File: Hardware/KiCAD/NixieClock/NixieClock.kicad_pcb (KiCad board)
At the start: 2 copper layers, 7 parts

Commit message: KiCAD Progress
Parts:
- removed REF** (x2): DIP-16_W10.16mm, Package_DIP:DIP-16_W10.16mm
- J0, J1: renamed from REF**; value Molex_Mini-Fit_Jr_5566-12A_2x06_P4.20mm_Vertical -> (none)
- moved IC0 0.49 mm to (55.3, 58.4)
- moved IC2 0.49 mm to (15.3, 58.4)
- moved IC1 0.49 mm to (35.7, 78.7)
- renumbered REF** to IC0, REF** to IC1, REF** to IC2
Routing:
- net (no net): track 4.03 -> 143.6 mm, vias 0 -> 1

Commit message: progress
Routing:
- net (no net): track 143.6 -> 300.5 mm

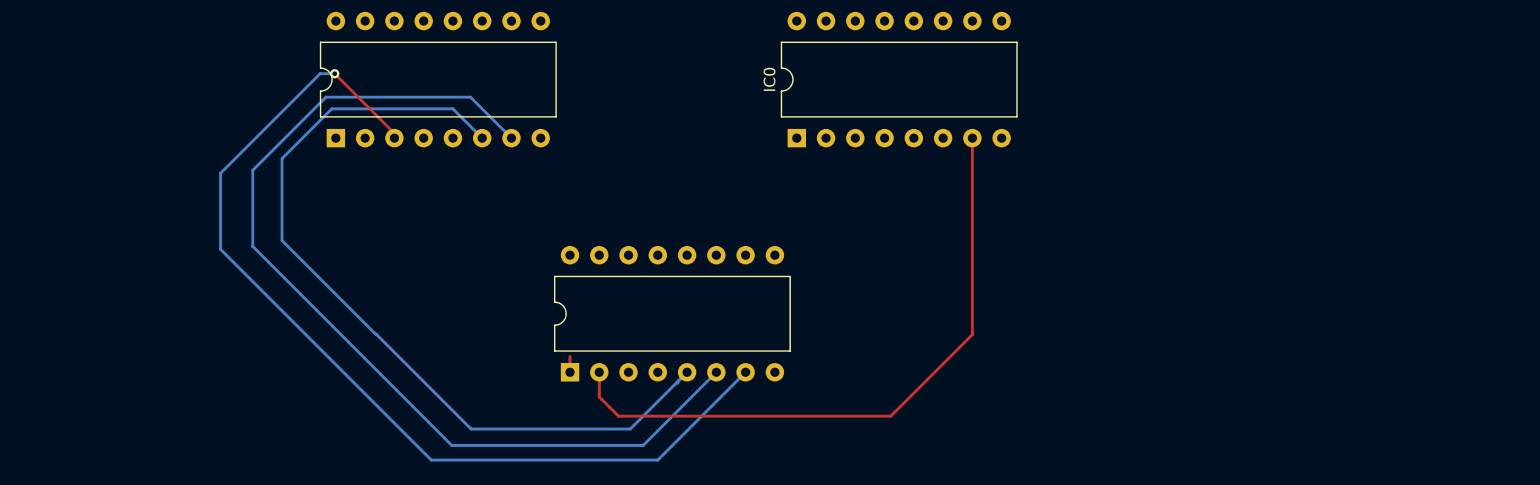
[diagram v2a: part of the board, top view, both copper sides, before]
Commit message: Routed from one shift register to BCD.. removed gound and vcc on eagle
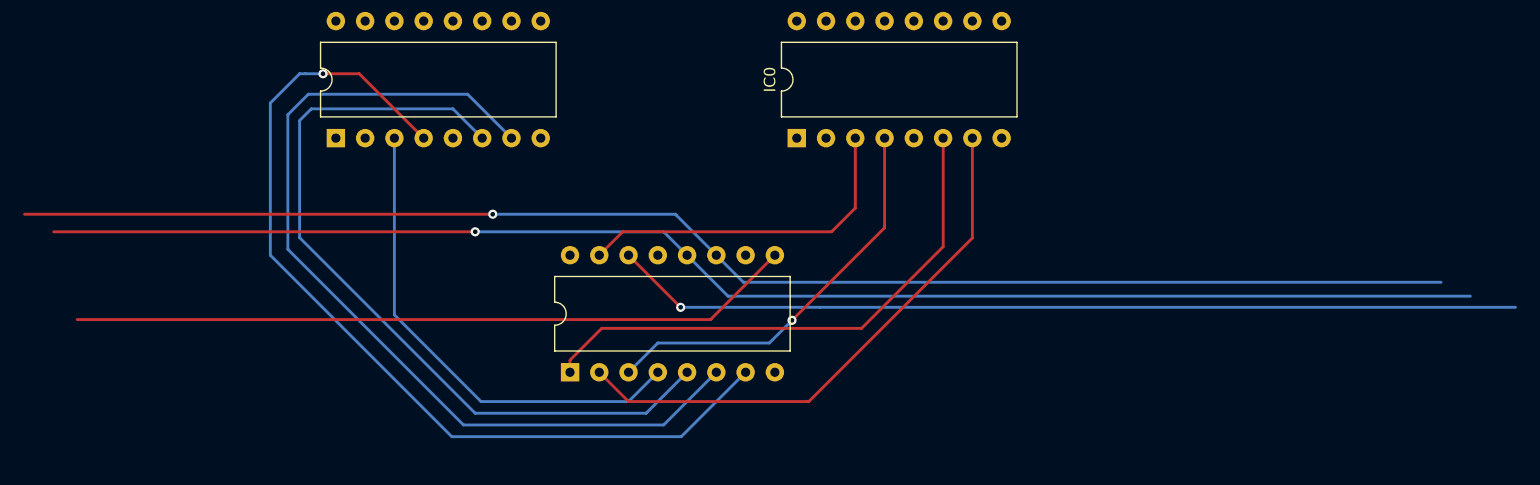
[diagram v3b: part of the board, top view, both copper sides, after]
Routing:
- net (no net): track 300.5 -> 827.0 mm, vias 1 -> 5
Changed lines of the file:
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@@
-(kicad_pcb (version 20171130) (host pcbnew "(5.1.4-0-10_14)")
+(kicad_pcb (version 20171130) (host pcbnew "(5.1.4)-1")
   (general
     (thickness 1.6)
     (drawings 0)
-    (tracks 36)
+    (tracks 73)
     (zones 0)
     (modules 5)
@@
   (segment (start 22.14 33.43) (end 23.74 33.43) (width 0.25) (layer F.Cu) (net 0))
   (segment (start 20.42 35.15) (end 22.14 33.43) (width 0.25) (layer F.Cu) (net 0))
-  (via (at 15.24 52.832) (size 0.8) (drill 0.4) (layers F.Cu B.Cu) (net 0))
-  (segment (start 45.020001 79.539999) (end 45.020001 79.693999) (width 0.25) (layer B.Cu) (net 0))
-  (segment (start 45.82 78.74) (end 45.020001 79.539999) (width 0.25) (layer B.Cu) (net 0))
-  (segment (start 13.97 52.832) (end 15.24 52.832) (width 0.25) (layer B.Cu) (net 0))
-  (segment (start 5.334 68.072) (end 5.334 61.468) (width 0.25) (layer B.Cu) (net 0))
-  (segment (start 23.622 86.36) (end 5.334 68.072) (width 0.25) (layer B.Cu) (net 0))
-  (segment (start 5.334 61.468) (end 13.97 52.832) (width 0.25) (layer B.Cu) (net 0))
-  (segment (start 43.28 86.36) (end 23.622 86.36) (width 0.25) (layer B.Cu) (net 0))
-  (segment (start 50.9 78.74) (end 43.28 86.36) (width 0.25) (layer B.Cu) (net 0))
-  (segment (start 8.128 61.214) (end 14.478 54.864) (width 0.25) (layer B.Cu) (net 0))
-  (segment (start 8.128 67.818) (end 8.128 61.214) (width 0.25) (layer B.Cu) (net 0))
-  (segment (start 42.01 85.09) (end 25.4 85.09) (width 0.25) (layer B.Cu) (net 0))
-  (segment (start 25.4 85.09) (end 8.128 67.818) (width 0.25) (layer B.Cu) (net 0))
-  (segment (start 48.36 78.74) (end 42.01 85.09) (width 0.25) (layer B.Cu) (net 0))
-  (segment (start 14.986 55.88) (end 25.5 55.88) (width 0.25) (layer B.Cu) (net 0))
-  (segment (start 10.668 67.31) (end 10.668 60.198) (width 0.25) (layer B.Cu) (net 0))
-  (segment (start 18.85 75.438) (end 18.796 75.438) (width 0.25) (layer B.Cu) (net 0))
-  (segment (start 27.078 83.666) (end 18.85 75.438) (width 0.25) (layer B.Cu) (net 0))
-  (segment (start 18.796 75.438) (end 10.668 67.31) (width 0.25) (layer B.Cu) (net 0))
+  (via (at 14.224 52.832) (size 0.8) (drill 0.4) (layers F.Cu B.Cu) (net 0))
+  (segment (start 20.42 58.012) (end 20.42 58.42) (width 0.25) (layer F.Cu) (net 0))
+  (segment (start 26.77 54.61) (end 30.58 58.42) (width 0.25) (layer B.Cu) (net 0))
+  (segment (start 43.28 78.74) (end 40.74 81.28) (width 0.25) (layer B.Cu) (net 0))
+  (segment (start 20.42 73.76) (end 20.42 58.42) (width 0.25) (layer B.Cu) (net 0))
+  (segment (start 17.372 52.832) (end 22.96 58.42) (width 0.25) (layer F.Cu) (net 0))
+  (segment (start 68.04 67.85) (end 68.04 58.42) (width 0.25) (layer F.Cu) (net 0))
+  (segment (start 60.96 74.93) (end 68.04 67.85) (width 0.25) (layer F.Cu) (net 0))
+  (segment (start 38.42 74.93) (end 60.96 74.93) (width 0.25) (layer F.Cu) (net 0))
+  (segment (start 35.66 78.74) (end 35.66 77.69) (width 0.25) (layer F.Cu) (net 0))
+  (segment (start 35.66 77.69) (end 38.42 74.93) (width 0.25) (layer F.Cu) (net 0))
+  (segment (start 45.312 73.152) (end 45.262 73.102) (width 0.25) (layer F.Cu) (net 0))
+  (segment (start 45.82 68.58) (end 43.788 66.548) (width 0.25) (layer B.Cu) (net 0))
+  (segment (start 43.788 66.548) (end 27.432 66.548) (width 0.25) (layer B.Cu) (net 0))
+  (via (at 27.432 66.548) (size 0.8) (drill 0.4) (layers F.Cu B.Cu) (net 0))
+  (segment (start 27.432 66.548) (end -9.144 66.548) (width 0.25) (layer F.Cu) (net 0))
+  (via (at 28.956 65.024) (size 0.8) (drill 0.4) (layers F.Cu B.Cu) (net 0))
+  (segment (start 28.956 65.024) (end -11.684 65.024) (width 0.25) (layer F.Cu) (net 0))
+  (segment (start 40.74 81.28) (end 38.2 78.74) (width 0.25) (layer F.Cu) (net 0))
+  (segment (start 40.74 78.74) (end 43.28 76.2) (width 0.25) (layer B.Cu) (net 0))
+  (via (at 54.9275 74.2315) (size 0.8) (drill 0.4) (layers F.Cu B.Cu) (net 0))
+  (segment (start 40.74 81.28) (end 56.388 81.28) (width 0.25) (layer F.Cu) (net 0))
+  (segment (start 70.58 67.088) (end 70.58 58.42) (width 0.25) (layer F.Cu) (net 0))
+  (segment (start 56.388 81.28) (end 70.58 67.088) (width 0.25) (layer F.Cu) (net 0))
+  (segment (start 48.36 78.74) (end 43.788 83.312) (width 0.25) (layer B.Cu) (net 0))
+  (segment (start 43.788 83.312) (end 26.416 83.312) (width 0.25) (layer B.Cu) (net 0))
+  (segment (start 26.416 83.312) (end 11.176 68.072) (width 0.25) (layer B.Cu) (net 0))
+  (segment (start 11.176 56.388) (end 12.954 54.61) (width 0.25) (layer B.Cu) (net 0))
+  (segment (start 11.176 68.072) (end 11.176 56.388) (width 0.25) (layer B.Cu) (net 0))
+  (segment (start 12.954 54.61) (end 26.77 54.61) (width 0.25) (layer B.Cu) (net 0))
+  (segment (start 17.372 52.832) (end 14.224 52.832) (width 0.25) (layer F.Cu) (net 0))
+  (segment (start 45.262 73.102) (end 40.74 68.58) (width 0.25) (layer F.Cu) (net 0))
+  (via (at 45.262 73.102) (size 0.8) (drill 0.4) (layers F.Cu B.Cu) (net 0))
+  (segment (start 47.879 74.141) (end 47.879 74.168) (width 0.25) (layer F.Cu) (net 0))
+  (segment (start 53.44 68.58) (end 47.879 74.141) (width 0.25) (layer F.Cu) (net 0))
+  (segment (start 47.879 74.168) (end -7.112 74.168) (width 0.25) (layer F.Cu) (net 0))
+  (segment (start 27.94 81.28) (end 20.42 73.76) (width 0.25) (layer B.Cu) (net 0))
+  (segment (start 40.74 81.28) (end 27.94 81.28) (width 0.25) (layer B.Cu) (net 0))
   (segment (start 25.5 55.88) (end 28.04 58.42) (width 0.25) (layer B.Cu) (net 0))
-  (segment (start 10.668 60.198) (end 14.986 55.88) (width 0.25) (layer B.Cu) (net 0))
-  (segment (start 40.894 83.666) (end 27.078 83.666) (width 0.25) (layer B.Cu) (net 0))
-  (segment (start 45.82 78.74) (end 40.894 83.666) (width 0.25) (layer B.Cu) (net 0))
-  (segment (start 27.024 54.864) (end 30.58 58.42) (width 0.25) (layer B.Cu) (net 0))
-  (segment (start 14.478 54.864) (end 27.024 54.864) (width 0.25) (layer B.Cu) (net 0))
-  (segment (start 20.42 58.012) (end 20.42 58.42) (width 0.25) (layer F.Cu) (net 0))
-  (segment (start 15.24 52.832) (end 20.42 58.012) (width 0.25) (layer F.Cu) (net 0))
-  (segment (start 35.66 78.74) (end 35.66 77.37) (width 0.25) (layer F.Cu) (net 0))
-  (segment (start 63.5 82.55) (end 39.878 82.55) (width 0.25) (layer F.Cu) (net 0))
-  (segment (start 70.58 75.406) (end 70.612 75.438) (width 0.25) (layer F.Cu) (net 0))
-  (segment (start 39.878 82.55) (end 38.2 80.872) (width 0.25) (layer F.Cu) (net 0))
-  (segment (start 70.612 75.438) (end 63.5 82.55) (width 0.25) (layer F.Cu) (net 0))
-  (segment (start 38.2 80.872) (end 38.2 78.74) (width 0.25) (layer F.Cu) (net 0))
-  (segment (start 70.58 58.42) (end 70.58 75.406) (width 0.25) (layer F.Cu) (net 0))
+  (segment (start 42.264 82.296) (end 27.432 82.296) (width 0.25) (layer B.Cu) (net 0))
+  (segment (start 45.82 78.74) (end 42.264 82.296) (width 0.25) (layer B.Cu) (net 0))
+  (segment (start 27.432 82.296) (end 12.192 67.056) (width 0.25) (layer B.Cu) (net 0))
+  (segment (start 12.192 67.056) (end 12.192 56.896) (width 0.25) (layer B.Cu) (net 0))
+  (segment (start 12.192 56.896) (end 13.208 55.88) (width 0.25) (layer B.Cu) (net 0))
+  (segment (start 13.208 55.88) (end 25.5 55.88) (width 0.25) (layer B.Cu) (net 0))
+  (segment (start 12.7 52.832) (end 14.224 52.832) (width 0.25) (layer B.Cu) (net 0))
+  (segment (start 45.312 84.328) (end 25.4 84.328) (width 0.25) (layer B.Cu) (net 0))
+  (segment (start 50.9 78.74) (end 45.312 84.328) (width 0.25) (layer B.Cu) (net 0))
+  (segment (start 25.4 84.328) (end 9.652 68.58) (width 0.25) (layer B.Cu) (net 0))
+  (segment (start 9.652 68.58) (end 9.652 55.372) (width 0.25) (layer B.Cu) (net 0))
+  (segment (start 9.652 55.372) (end 12.192 52.832) (width 0.25) (layer B.Cu) (net 0))
+  (segment (start 12.192 52.832) (end 12.7 52.832) (width 0.25) (layer B.Cu) (net 0))
+  (segment (start 45.262 73.102) (end 57.354 73.102) (width 0.25) (layer B.Cu) (net 0))
+  (segment (start 57.354 73.102) (end 117.7155 73.102) (width 0.25) (layer B.Cu) (net 0))
+  (segment (start 52.959 76.2) (end 54.9275 74.2315) (width 0.25) (layer B.Cu) (net 0))
+  (segment (start 43.28 76.2) (end 52.959 76.2) (width 0.25) (layer B.Cu) (net 0))
+  (segment (start 62.96 66.199) (end 62.96 66.072) (width 0.25) (layer F.Cu) (net 0))
+  (segment (start 54.9275 74.2315) (end 62.96 66.199) (width 0.25) (layer F.Cu) (net 0))
+  (segment (start 62.96 66.072) (end 62.96 58.42) (width 0.25) (layer F.Cu) (net 0))
+  (segment (start 60.42 64.484) (end 60.42 58.42) (width 0.25) (layer F.Cu) (net 0))
+  (segment (start 58.356 66.548) (end 60.42 64.484) (width 0.25) (layer F.Cu) (net 0))
+  (segment (start 38.2 68.58) (end 40.232 66.548) (width 0.25) (layer F.Cu) (net 0))
+  (segment (start 40.232 66.548) (end 58.356 66.548) (width 0.25) (layer F.Cu) (net 0))
+  (segment (start 49.376 72.136) (end 49.911 72.136) (width 0.25) (layer B.Cu) (net 0))
+  (segment (start 45.82 68.58) (end 49.376 72.136) (width 0.25) (layer B.Cu) (net 0))
+  (segment (start 49.911 72.136) (end 113.792 72.136) (width 0.25) (layer B.Cu) (net 0))
+  (segment (start 48.36 68.58) (end 50.7095 70.9295) (width 0.25) (layer B.Cu) (net 0))
+  (segment (start 50.7095 70.9295) (end 111.252 70.9295) (width 0.25) (layer B.Cu) (net 0))
+  (segment (start 44.804 65.024) (end 44.881 65.101) (width 0.25) (layer B.Cu) (net 0))
+  (segment (start 28.956 65.024) (end 44.804 65.024) (width 0.25) (layer B.Cu) (net 0))
+  (segment (start 48.36 68.58) (end 44.881 65.101) (width 0.25) (layer B.Cu) (net 0))
 )

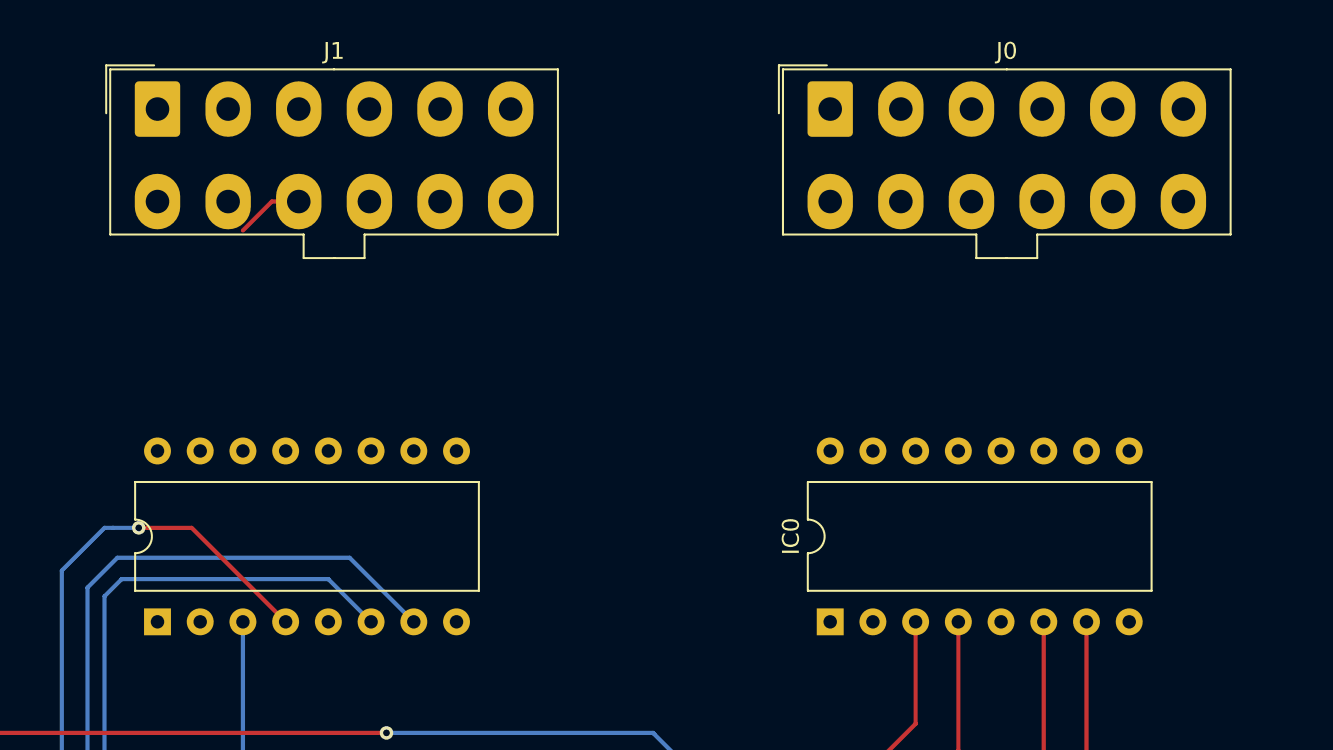
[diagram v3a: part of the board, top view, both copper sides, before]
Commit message: Renamed pins on shift register in kicad
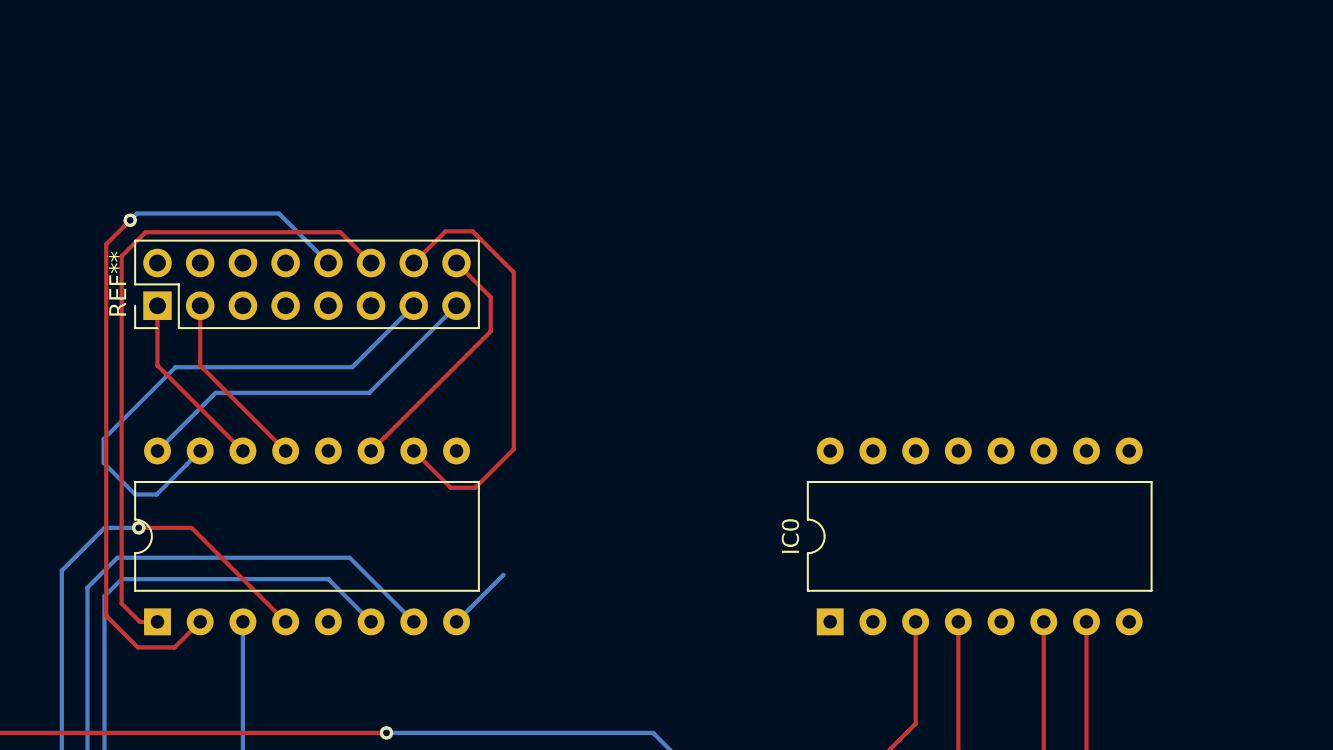
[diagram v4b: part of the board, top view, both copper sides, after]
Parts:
- removed J0, J1: , Connector_Molex:Molex_Mini-Fit_Jr_5566-12A_2x06_P4.20mm_Vertical
- added REF**: , Connector_PinHeader_2.54mm:PinHeader_2x08_P2.54mm_Vertical, F.Cu at (15.3, 39.6)
- IC0, IC1, IC2: value DIP-16_W10.16mm -> (none)
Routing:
- net (no net): track 827.0 -> 1025.2 mm, vias 5 -> 6

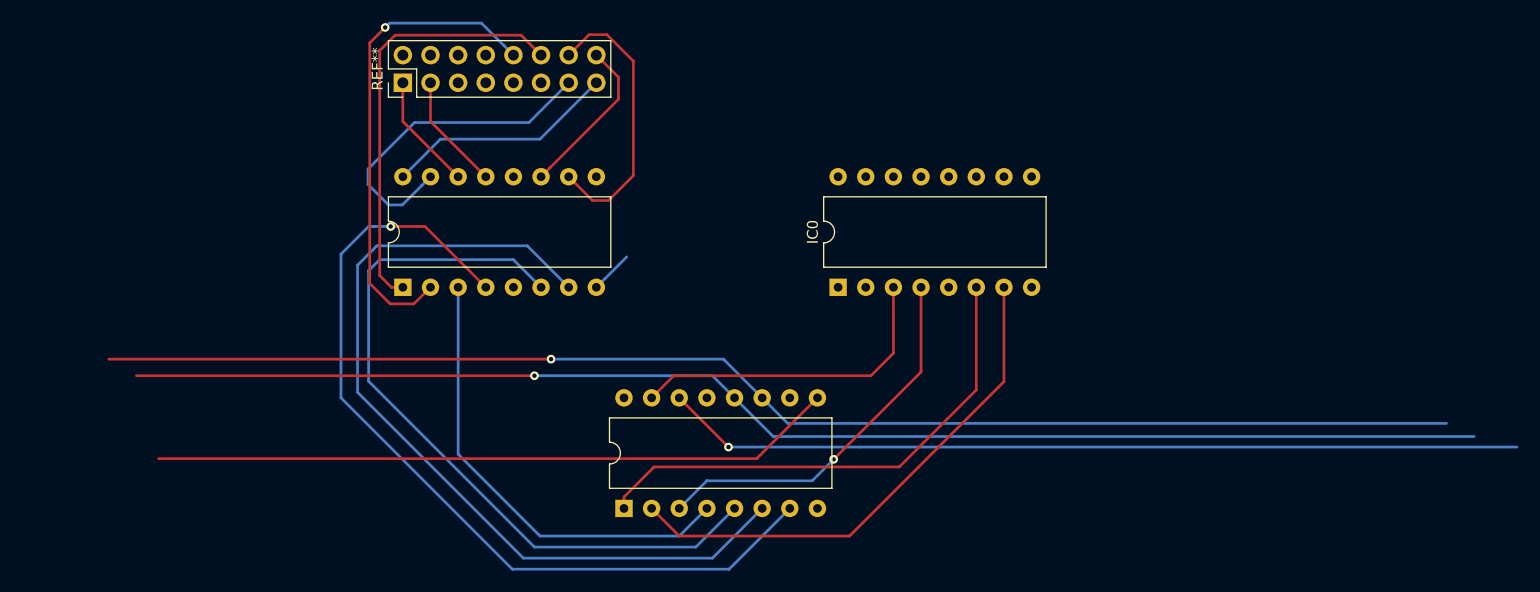
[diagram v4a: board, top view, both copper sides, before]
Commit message: Made datasheet folder.. fixed routing between SR and BCDs.
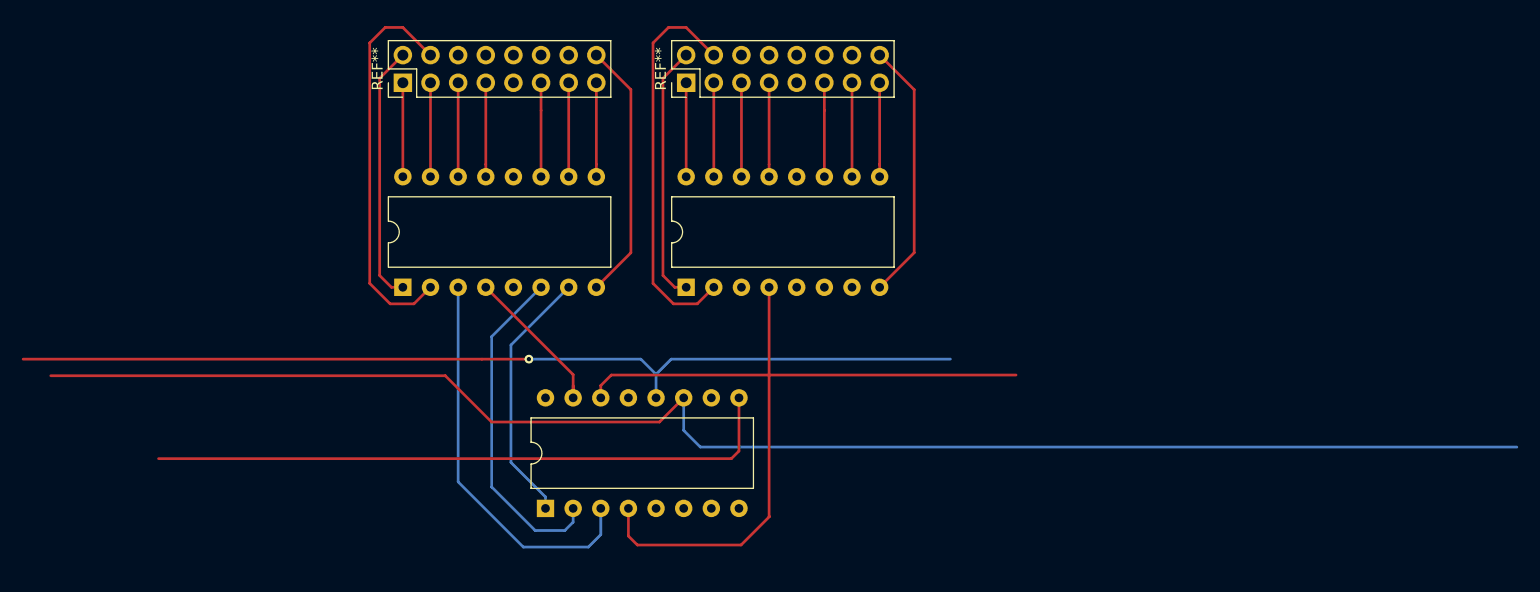
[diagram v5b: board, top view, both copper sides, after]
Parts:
- removed IC0: , Package_DIP:DIP-16_W10.16mm
- added IC2: , Package_DIP:DIP-16_W10.16mm, F.Cu at (41.4, 58.4)
- added REF**: , Connector_PinHeader_2.54mm:PinHeader_2x08_P2.54mm_Vertical, F.Cu at (41.4, 39.6)
- moved IC1 7.21 mm to (28.4, 78.7)
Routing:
- net (no net): track 1025.2 -> 761.3 mm, vias 6 -> 1

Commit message: Finished routing one complete stage... Now trying to make a kicad sch
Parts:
- moved IC2 176.5 mm to (185.5, 105.2)
- moved IC2 176.5 mm to (211.6, 105.2)
- moved REF** 176.5 mm to (211.6, 86.4)
- moved REF** 176.5 mm to (185.5, 86.4)
- moved IC1 176.5 mm to (198.6, 125.5)
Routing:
- net (no net): track 761.3 -> 1545.3 mm, vias 1 -> 2
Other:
- board outline added: 53.3 x 58.4 mm

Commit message: Progress
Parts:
- added REF**: NODE MCU, NixieClock:NODEMCU, F.Cu at (254.5, 114.0)
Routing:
- net (no net): track 1545.3 -> 1473.9 mm, vias 2 -> 4
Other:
- board outline removed

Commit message: Progress.. about to duplicate to 3 stages
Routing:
- net (no net): track 1473.9 -> 1469.5 mm, vias 4 -> 3
